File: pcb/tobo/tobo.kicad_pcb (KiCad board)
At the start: 2 copper layers, 57.5 x 61 mm, 88 parts, among them J1 Molex 538-54548-2272, J2 Conn_01x02_Pin, J4 Molex 538-54548-2472, J5 Conn_01x09_Pin, J6 Conn_01x09_Pin, J7 Conn_01x09_Pin, J8 Hroparts Elec TYPE-C-31-M-12, U1 TS5A23167, U10 5015, U11 5015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

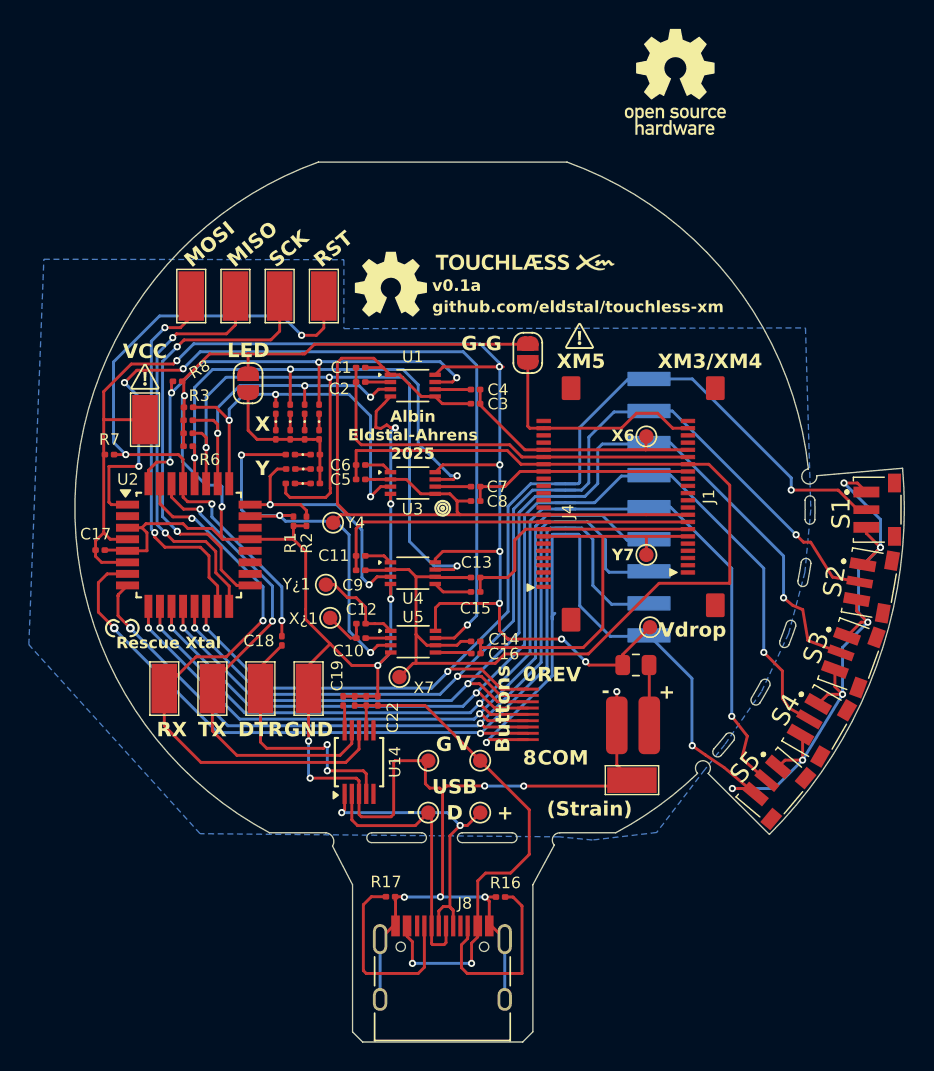
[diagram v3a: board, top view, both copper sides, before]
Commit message: Confirmed pinouts of XM5 and XM5.
Experimental support for XM2 added.
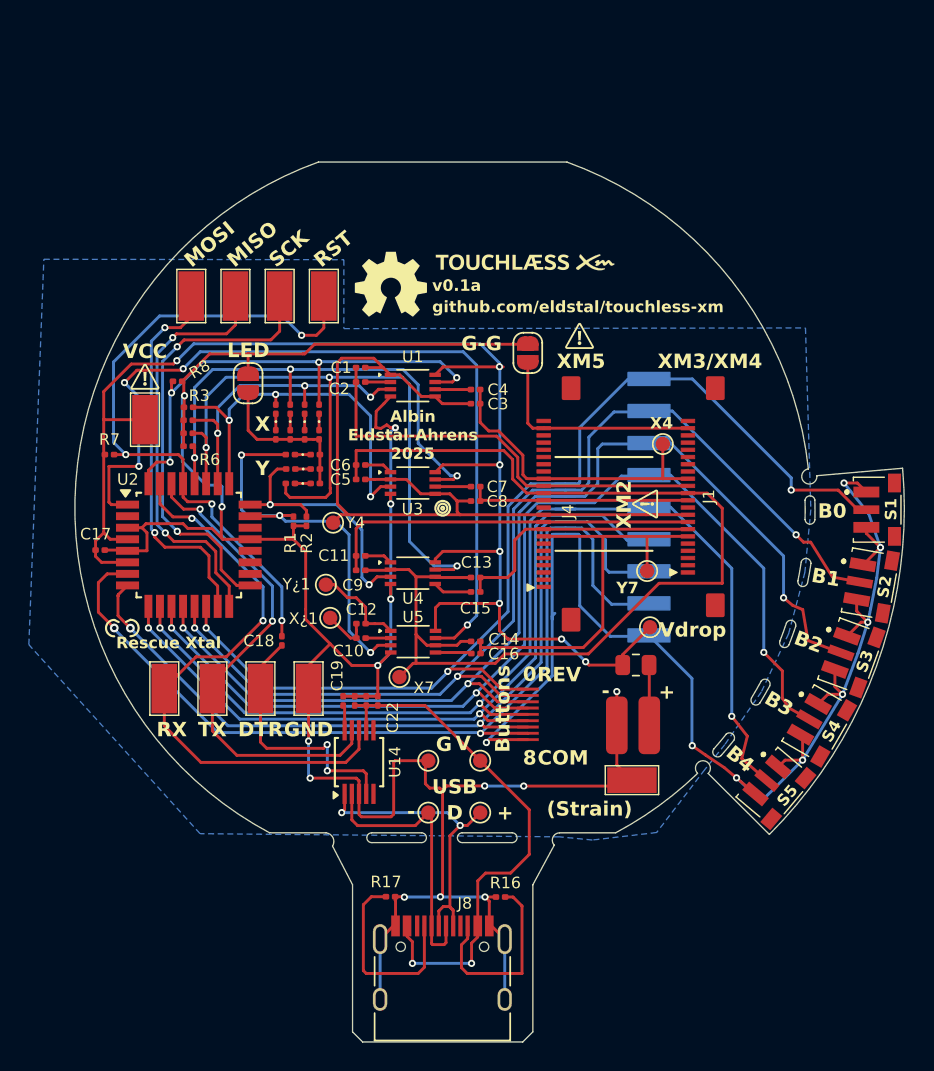
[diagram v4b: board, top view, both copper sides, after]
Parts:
- moved X1 1.26 mm to (155.3, 85.5)
- moved X2 1.12 mm to (154.2, 94.3)
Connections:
- net /5,4 renamed /3,4
- net /6,4 renamed /4,4
- net /7,4 renamed /2,4
- net /8,4 renamed /1,4
- C1 pad 2: /X5 -> /X3
- C13 pad 1: /X7 -> /X2
- C14 pad 1: /X7 -> /X2
- C2 pad 1: /X5 -> /X3
- C3 pad 1: /X6 -> /X4
- C4 pad 2: /X6 -> /X4
- C5 pad 1: /X7 -> /X2
- C6 pad 2: /X7 -> /X2
- C7 pad 2: /X8 -> /X1
- C8 pad 1: /X8 -> /X1
- C9 pad 2: /X7 -> /X2
- J1 pad 11: unconnected-(J1-X1-Pad11) -> /X1
- J1 pad 12: unconnected-(J1-X2-Pad12) -> /X2
- J1 pad 13: unconnected-(J1-X3-Pad13) -> /X3
- J1 pad 14: unconnected-(J1-X4-Pad14) -> /X4
- J1 pad 15: /X8 -> unconnected-(J1-X8-Pad15)
- J1 pad 16: /X7 -> unconnected-(J1-X7-Pad16)
- J1 pad 17: /X5 -> unconnected-(J1-X5-Pad17)
- J1 pad 18: /X6 -> unconnected-(J1-X6-Pad18)
- J4 pad 13: unconnected-(J4-X1?-Pad13) -> /X1
- J4 pad 14: unconnected-(J4-X2?-Pad14) -> /X2
- J4 pad 15: unconnected-(J4-X3-Pad15) -> /X3
- J4 pad 16: unconnected-(J4-X4-Pad16) -> /X4
- J4 pad 17: /X8 -> unconnected-(J4-X8-Pad17)
- J4 pad 18: /X7 -> unconnected-(J4-X7-Pad18)
- J4 pad 19: /X5 -> unconnected-(J4-X5-Pad19)
- J4 pad 20: /X6 -> unconnected-(J4-X6-Pad20)
- U4 pad 2: /X7 -> /X2
- U4 pad 6: /X7 -> /X2
- U5 pad 6: /X7 -> /X2
- X1 pad 1: /X6 -> /X4
- X7 pad 1: /X7 -> /X2
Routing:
- net /X7: track 79.1 -> 0.00 mm
- net /X2: track 0.00 -> 77.9 mm
- net /X3: track 0.00 -> 30.0 mm
- net /X5: track 28.5 -> 0.00 mm
- net /X4: track 0.00 -> 21.6 mm
- net /X6: track 17.7 -> 0.00 mm
- net /X8: track 15.8 -> 0.00 mm
- net /X1: track 0.00 -> 15.4 mm
- net GND: track 273.6 -> 271.5 mm
- net /Y7: track 27.5 -> 28.7 mm
- net Net-(J1-GND): track 16.5 -> 15.5 mm
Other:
- board text added: "B0"
- board text added: "B1"
- board text added: "B2"
- board text added: "B3"
- board text added: "B4"
- board text added: "X4"
- board text added: "XM2"
- board text removed: "X6"

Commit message: PCB and documentation tweaks
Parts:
- moved R16 2.28 mm to (141.7, 116.8), turned to 90 degrees
- moved R17 1.57 mm to (137.9, 117.0), turned to 180 degrees
- renumbered X7 to X2
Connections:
- net /7,5 renamed /2,5
- net /7,6 renamed /2,6
- net /7,7 renamed /2,7
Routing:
- net Net-(J8-CC2): track 13.5 -> 1.83 mm
- net Net-(J8-CC1): track 13.7 -> 2.20 mm
- net GND: track 271.5 -> 274.1 mm, vias 22 -> 23

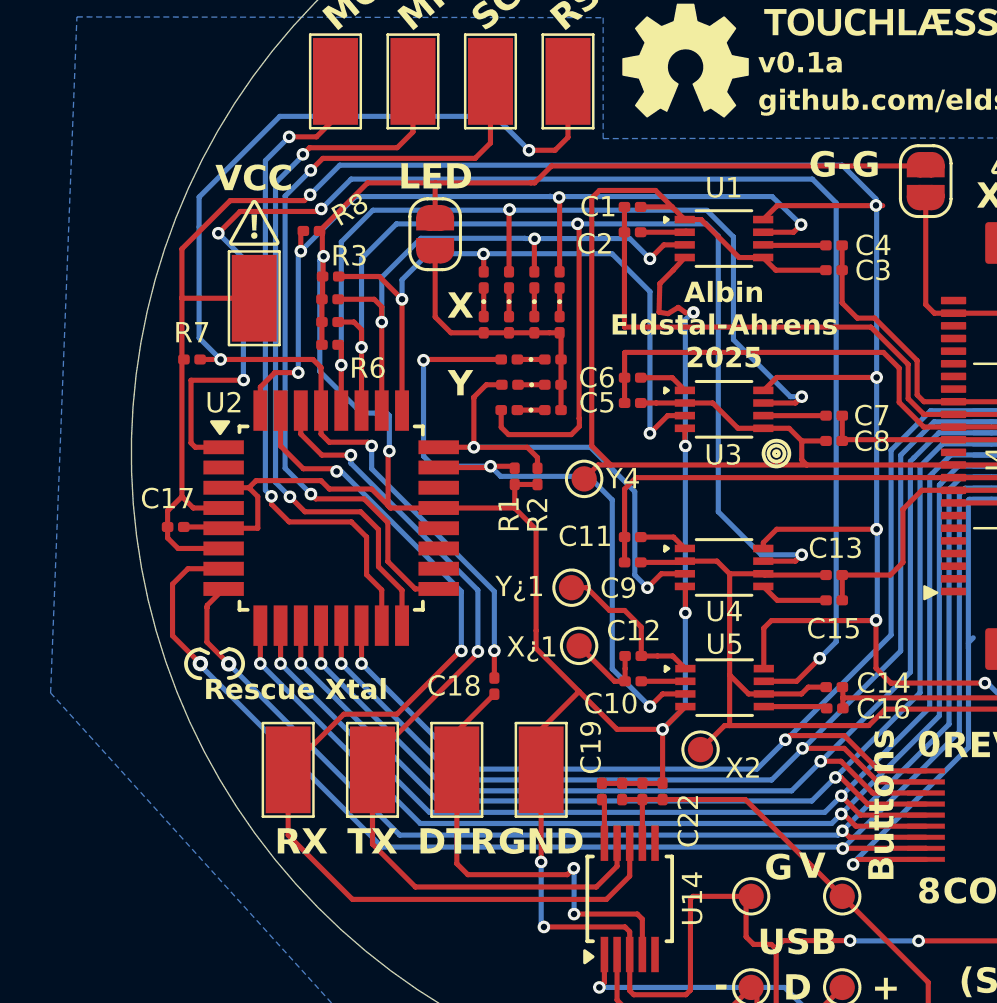
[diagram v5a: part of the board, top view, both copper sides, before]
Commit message: Swapped some GPIO to avoid PCINT problems
This lead to a tasty basket weave of traces under the MCU, but that's
fine I guess.

The only reason this change was "necessary" is because regular arduino
doesn't expose gpio on the crystal pins. Therefore the PCINT libraries
don't seem to support enabling the pin change interrupt on those pins.

It was neat to have them as buttons, from a routing perspective, but
this should -work- which seems more important.
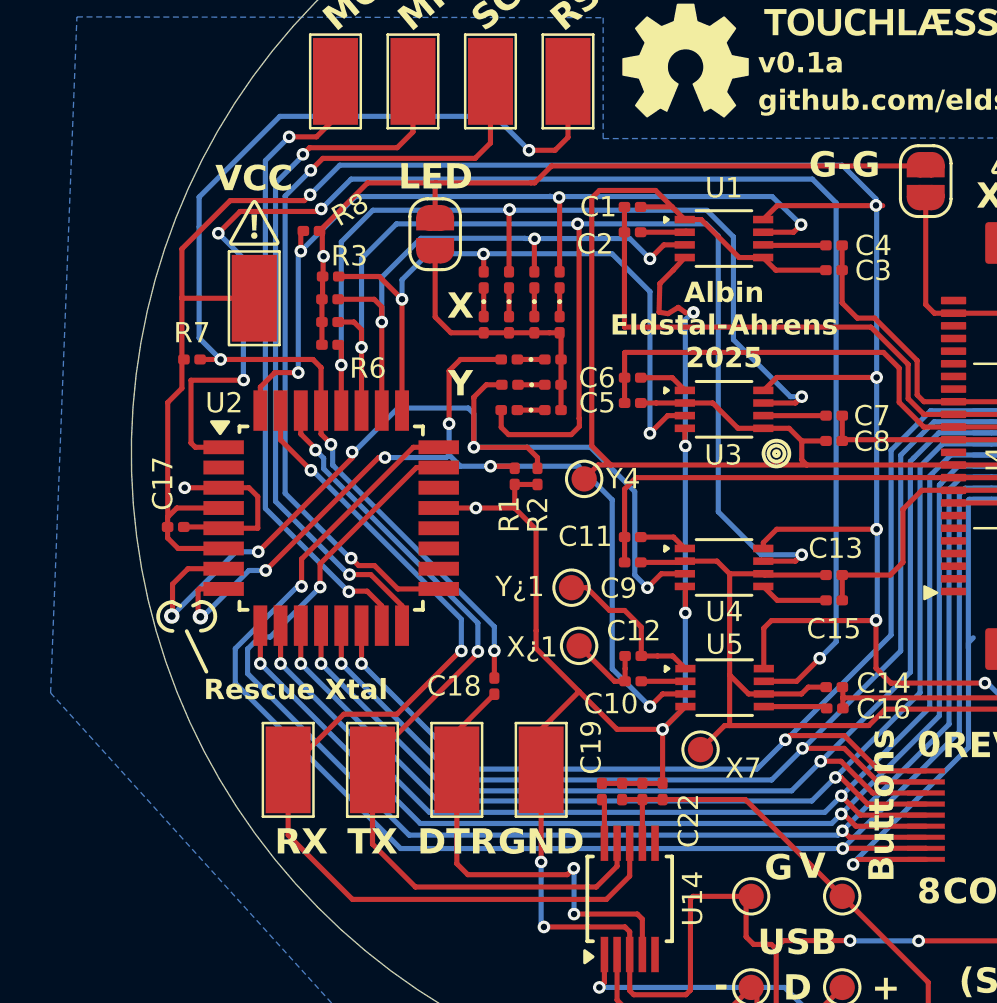
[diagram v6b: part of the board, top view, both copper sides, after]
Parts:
- renumbered X2 to X7
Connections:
- U2 pad 23: /2,7 -> /BTN6
- U2 pad 24: /2,6 -> /BTN7
- U2 pad 7: /BTN7 -> /2,6
- U2 pad 8: /BTN6 -> /2,7
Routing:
- net /2,6: track 20.6 -> 39.7 mm, vias 2 -> 5
- net GND: track 274.1 -> 255.8 mm, vias 23 -> 24
- net /2,7: track 28.6 -> 38.9 mm, vias 3 -> 6
- net /BTN6: track 59.7 -> 67.2 mm
- net /BTN7: track 64.8 -> 70.5 mm
- net /MOSI: track 26.6 -> 25.7 mm
- net /RESET: track 46.6 -> 45.7 mm
- net /RX: track 40.9 -> 40.1 mm
- net /MISO: track 29.2 -> 28.4 mm
- net /TX: track 34.0 -> 33.4 mm
- net +BATT: track 100.3 -> 100.8 mm

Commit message: Endless PCB tweaks
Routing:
- net GND: track 255.8 -> 261.2 mm, vias 24 -> 27
- net +BATT: track 100.8 -> 101.4 mm
- net /Y5: track 26.1 -> 25.5 mm

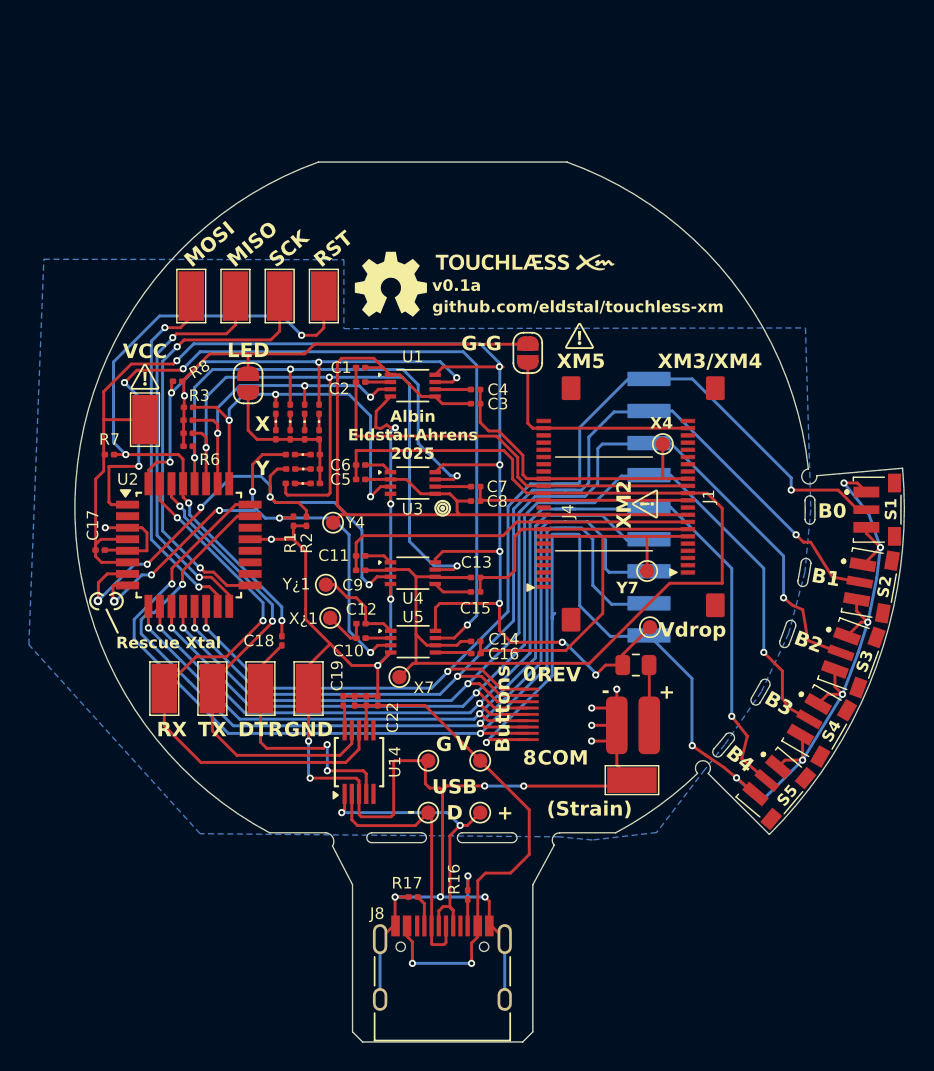
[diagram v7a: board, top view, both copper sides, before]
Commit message: Fixed order of Y LEDs
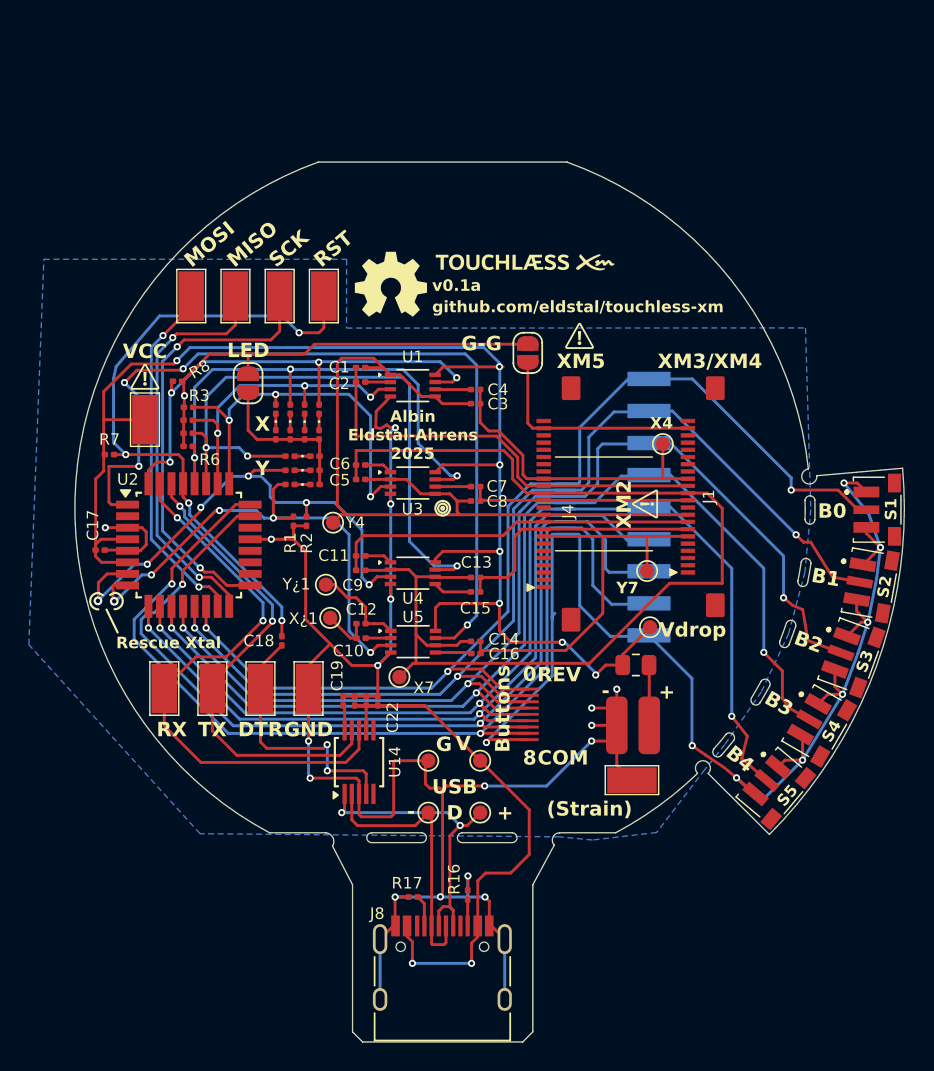
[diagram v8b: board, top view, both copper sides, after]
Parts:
- moved D1 2.07 mm to (129.4, 88.3)
- moved R9 2.07 mm to (131.1, 88.3)
- moved D5 1.89 mm to (129.4, 86.4)
- moved R13 1.89 mm to (131.1, 86.4)
- moved D2 0.10 mm to (129.4, 87.4)
- moved R10 0.09 mm to (131.1, 87.4)
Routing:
- net /2,5: track 51.1 -> 44.9 mm
- net /2,7: track 39.3 -> 36.7 mm, vias 6 -> 5
- net /2,6: track 39.4 -> 37.1 mm, vias 5 -> 6
- net GND: track 261.2 -> 259.7 mm, vias 27 -> 26
- net /MOSI: track 25.7 -> 25.0 mm
